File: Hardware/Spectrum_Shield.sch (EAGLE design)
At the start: 24 parts, among them IC1 MSGEQ7SOIC, IC2 MSGEQ7SOIC, U1 ARDUINO_R3_SHIELD

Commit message: computer change #2
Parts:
- removed JP1: LOGO-SFENEW, SparkFun:LOGO-SFENEW
- C1, C2, C3, C4: device SparkFun:CAP0402-CAP -> SparkFun-Capacitors:CAP0603-CAP
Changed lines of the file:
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@@
 <?xml version="1.0" encoding="utf-8"?>
 <!DOCTYPE eagle SYSTEM "eagle.dtd">
-<eagle version="6.4">
+<eagle version="6.5.0">
 <drawing>
 <settings>
@@
 </classes>
 <parts>
-<part name="C1" library="SparkFun" deviceset="CAP" device="0402-CAP" value="1000pF"/>
-<part name="C2" library="SparkFun" deviceset="CAP" device="0402-CAP" value="33pF"/>
+<part name="C1" library="SparkFun-Capacitors" deviceset="CAP" device="0603-CAP" value="1000pF"/>
+<part name="C2" library="SparkFun-Capacitors" deviceset="CAP" device="0603-CAP" value="33pF"/>
 <part name="C6" library="SparkFun-Capacitors" deviceset="0.1UF-25V(+80/-20%)(0603)" device="" value="0.1uF"/>
 <part name="R2" library="SparkFun-Resistors" deviceset="220KOHM1/10W1%(0603)" device="" value="200k"/>
@@
 <part name="GND5" library="SparkFun" deviceset="GND" device=""/>
 <part name="P+1" library="SparkFun" deviceset="VCC" device=""/>
-<part name="C3" library="SparkFun" deviceset="CAP" device="0402-CAP" value="1000pF"/>
-<part name="C4" library="SparkFun" deviceset="CAP" device="0402-CAP" value="33pF"/>
+<part name="C3" library="SparkFun-Capacitors" deviceset="CAP" device="0603-CAP" value="1000pF"/>
+<part name="C4" library="SparkFun-Capacitors" deviceset="CAP" device="0603-CAP" value="33pF"/>
 <part name="C5" library="SparkFun-Capacitors" deviceset="0.1UF-25V(+80/-20%)(0603)" device="" value="0.1uF"/>
 <part name="R1" library="SparkFun-Resistors" deviceset="200KOHM1/10W1%(0603)" device="200K" value="200k"/>
@@
 <part name="U1" library="SparkFun-Boards" deviceset="ARDUINO_R3_SHIELD" device=""/>
 <part name="FRAME1" library="SparkFun" deviceset="FRAME-LETTER" device=""/>
-<part name="JP1" library="SparkFun" deviceset="LOGO-SFE" device="NEW"/>
 <part name="R3" library="SparkFun-Resistors" deviceset="330OHM1/10W1%(0603)" device="" value="330"/>
 <part name="LED1" library="SparkFun-LED" deviceset="LED-RED" device="0603" value="RED"/>
@@
 <instance part="FRAME1" gate="G$1" x="0" y="0"/>
 <instance part="FRAME1" gate="G$2" x="147.32" y="0"/>
-<instance part="JP1" gate="G$1" x="241.3" y="38.1"/>
 <instance part="R3" gate="G$1" x="152.4" y="119.38" rot="R90"/>
 <instance part="LED1" gate="G$1" x="152.4" y="109.22"/>

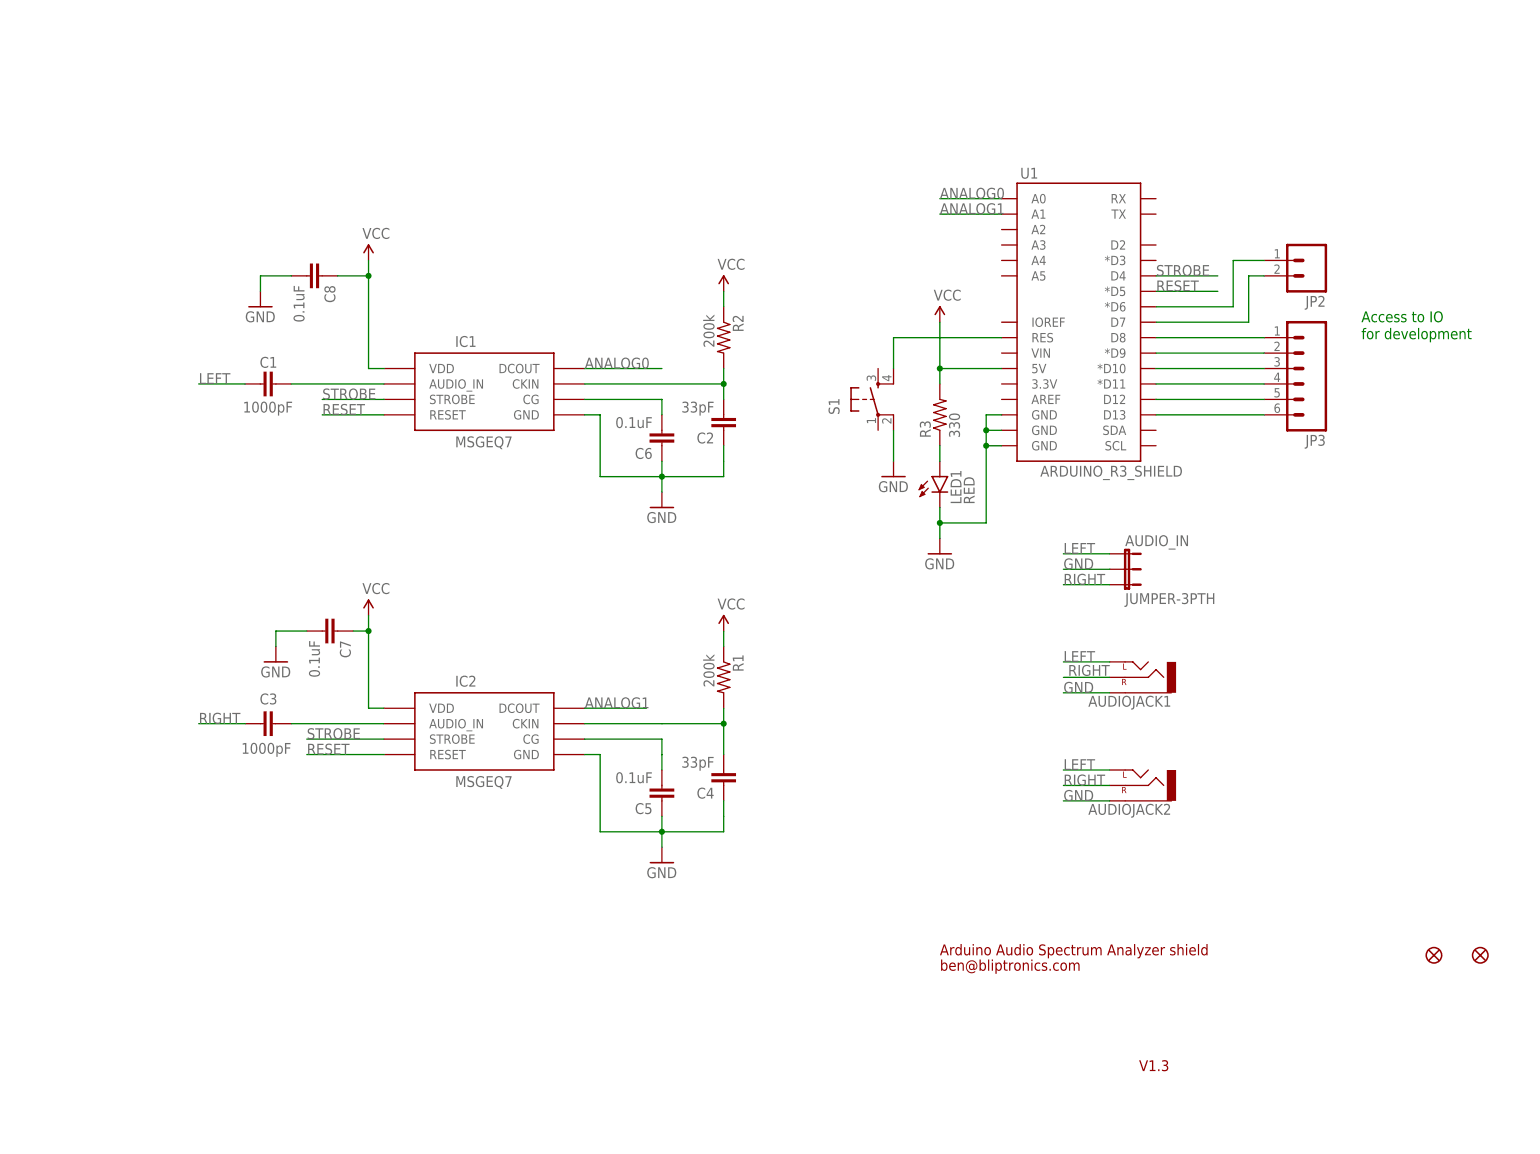
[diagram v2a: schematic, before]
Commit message: Fixed Sch, Added Input/Output Silk
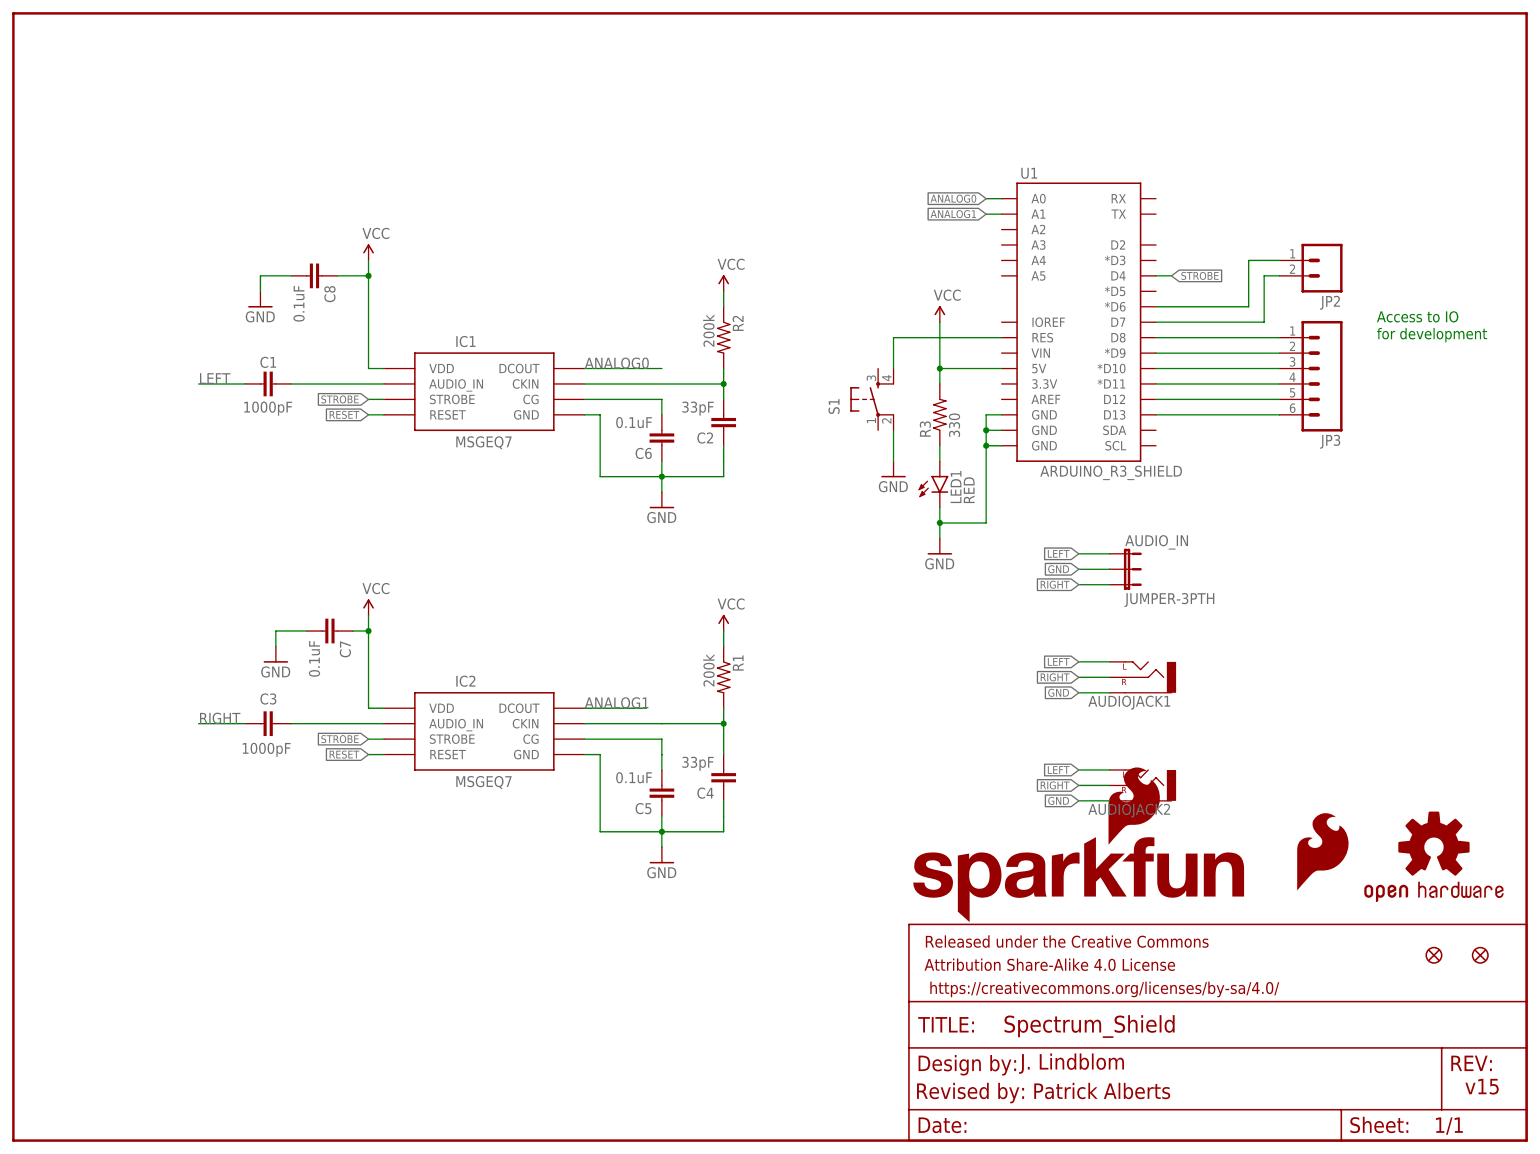
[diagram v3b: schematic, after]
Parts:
- added FRAME1: FRAME-LETTER, SparkFun-Aesthetics:FRAME-LETTER
- added LOGO1: OSHW-LOGOM, SparkFun-Aesthetics:OSHW-LOGOM
- added LOGO2: SFE_LOGO_FLAME.2_INCH, SparkFun-Aesthetics:SFE_LOGO_FLAME.2_INCH
- added LOGO3: SFE_LOGO_NAME_FLAME.1_INCH, SparkFun-Aesthetics:SFE_LOGO_NAME_FLAME.1_INCH
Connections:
- removed net N$8: JP2.1, U1.*D6
- net RESET: now also JP2.1, U1.*D6; no longer U1.*D5
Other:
- note added: "J. Lindblom"
- note added: "Revised by: Patrick Alberts"
- note added: "v15"
- note removed: "Arduino Audio Spectrum Analyzer shield"
- note removed: "V1.3"
- note removed: "ben@bliptronics.com"
- moved on the sheet: JP2, JP3
